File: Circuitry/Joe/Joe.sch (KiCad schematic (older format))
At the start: 42 parts

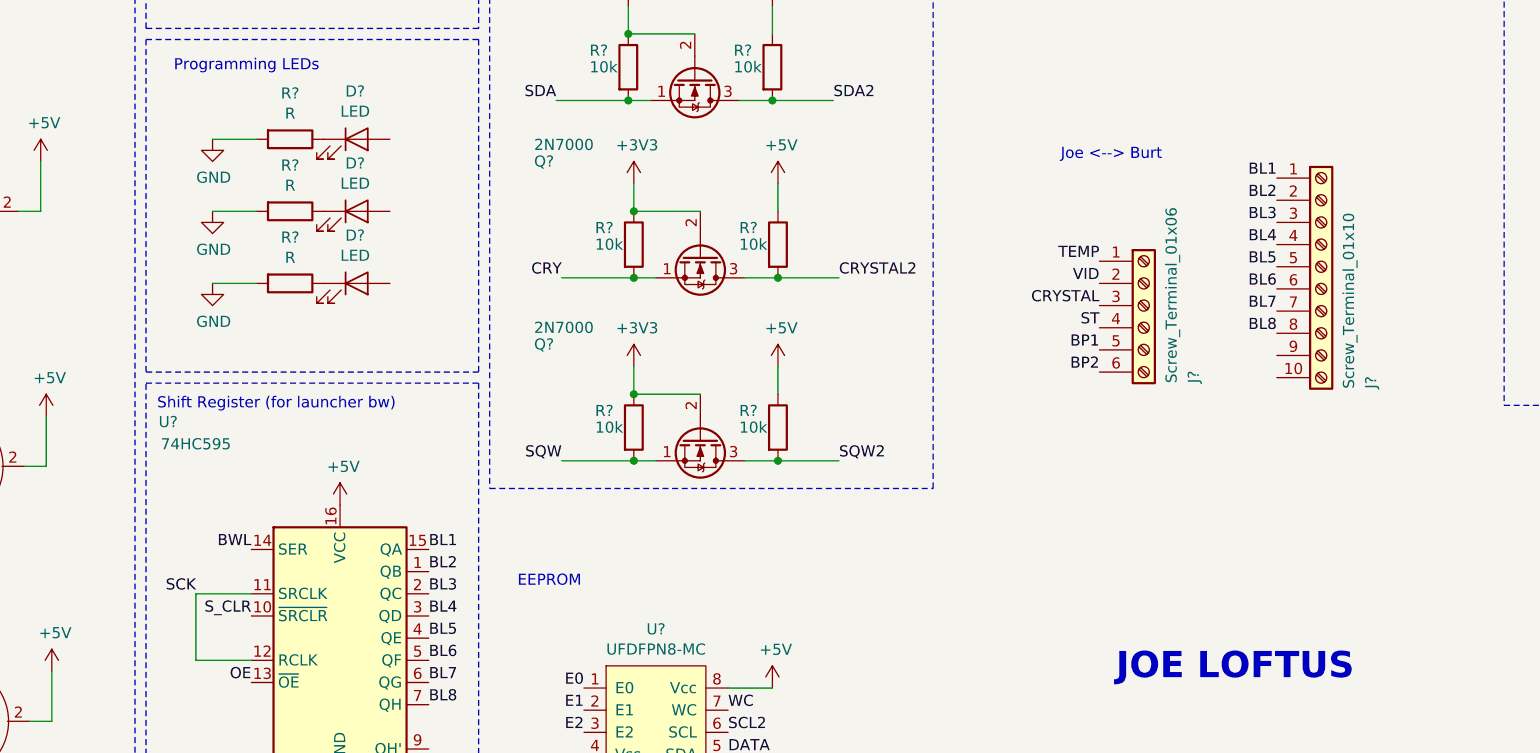
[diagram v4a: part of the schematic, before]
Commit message: shift reg to burt
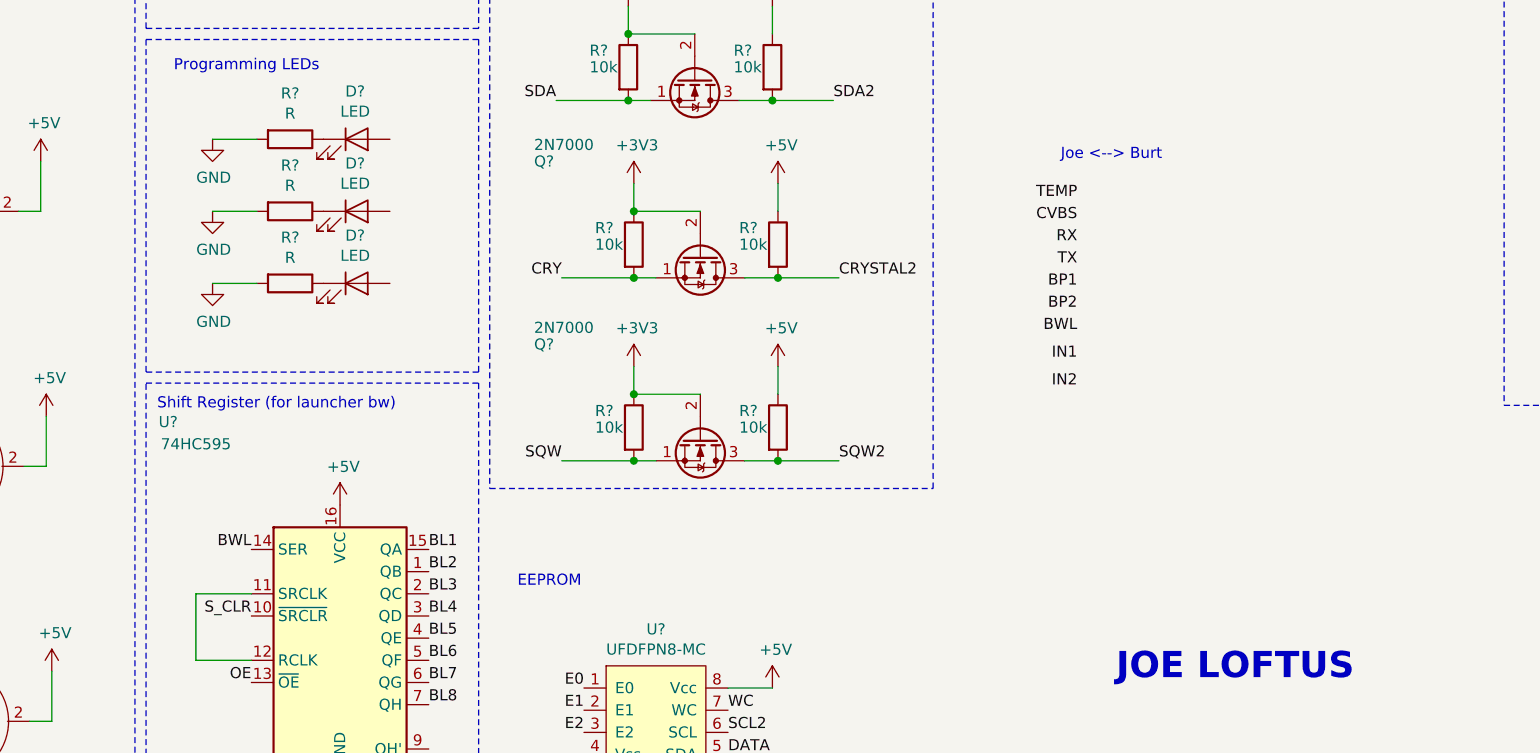
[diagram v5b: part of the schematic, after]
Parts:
- removed J?: Screw_Terminal_01x10, symbol Connector:Screw_Terminal_01x10
- removed J?: Screw_Terminal_01x06, symbol Connector:Screw_Terminal_01x06
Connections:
- net SCK: no longer U?.11 (SRCLK), U?.12 (RCLK)
- new net: U?.11 (SRCLK), U?.12 (RCLK)
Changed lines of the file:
@@
 Text Label 10875 3150 0    50   ~ 0
 PHO4
-Text Label 6950 4875 2    50   ~ 0
+Text Label 6850 4600 2    50   ~ 0
 TEMP
-Text Label 6950 5075 2    50   ~ 0
-CRYSTAL
+Text Label 6850 4800 2    50   ~ 0
+RX
 $Comp
 L power:+3V3 #PWR?
@@
 Wire Wire Line
 	10650 2450 10850 2450
-Text Label 6950 4975 2    50   ~ 0
-VID
-Text Label 6950 5175 2    50   ~ 0
-ST
+Text Label 6850 4700 2    50   ~ 0
+CVBS
+Text Label 6850 4900 2    50   ~ 0
+TX
 $Comp
 L Joe-rescue:UFDFPN8-MC-Custom U?
@@
 Wire Notes Line
 	2650 3875 2650 5375
-Text Label 2875 6375 2    50   ~ 0
-SCK
 Wire Wire Line
 	3125 6375 2875 6375
@@
 Wire Notes Line
 	6200 5900 6200 2475
-$Comp
-L Connector:Screw_Terminal_01x10 J?
-U 1 1 5D29FE3C
-P 7950 4900
-F 0 "J?" V 8175 4350 50  0000 L CNN
-F 1 "Screw_Terminal_01x10" V 8075 4350 50  0000 L CNN
-F 2 "" H 7950 4900 50  0001 C CNN
-F 3 "~" H 7950 4900 50  0001 C CNN
-	1    7950 4900
-	1    0    0    -1
-$EndComp
-$Comp
-L Connector:Screw_Terminal_01x06 J?
-U 1 1 5D2A1839
-P 7150 5075
-F 0 "J?" V 7375 4725 50  0000 L CNN
-F 1 "Screw_Terminal_01x06" V 7275 4725 50  0000 L CNN
-F 2 "" H 7150 5075 50  0001 C CNN
-F 3 "~" H 7150 5075 50  0001 C CNN
-	1    7150 5075
-	1    0    0    -1
-$EndComp
-Text Label 7750 4500 2    50   ~ 0
-BL1
-Text Label 7750 4600 2    50   ~ 0
-BL2
-Text Label 7750 4700 2    50   ~ 0
-BL3
-Text Label 7750 4800 2    50   ~ 0
-BL4
-Text Label 7750 4900 2    50   ~ 0
-BL5
-Text Label 7750 5000 2    50   ~ 0
-BL6
-Text Label 7750 5100 2    50   ~ 0
-BL7
-Text Label 7750 5200 2    50   ~ 0
-BL8
-Text Label 6950 5275 2    50   ~ 0
+Text Label 6850 5200 2    50   ~ 0
+BWL
+Text Label 6850 5000 2    50   ~ 0
 BP1
-Text Label 6950 5375 2    50   ~ 0
+Text Label 6850 5100 2    50   ~ 0
 BP2
+Text Label 6850 5325 2    50   ~ 0
+IN1
+Text Label 6850 5450 2    50   ~ 0
+IN2
 $EndSCHEMATC
